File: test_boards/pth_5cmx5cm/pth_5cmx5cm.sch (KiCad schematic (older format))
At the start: 4 parts, among them Q1 BC560, Q2 2N3904

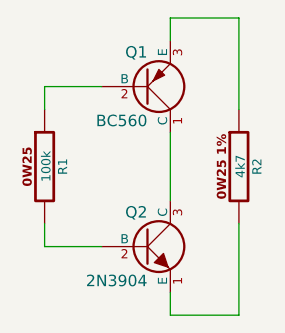
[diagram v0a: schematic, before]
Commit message: updating test board.
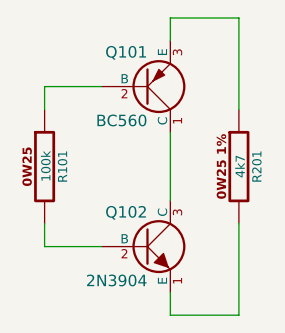
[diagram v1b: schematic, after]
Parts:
- removed Q1: BC560, ~, symbol BC560
- removed Q2: 2N3904, ~, symbol 2N3904
- added Q101: BC560, ~, symbol BC560
- added Q102: 2N3904, ~, symbol 2N3904
- renumbered R1 to R101, R2 to R201
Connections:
- net at R101.1: now also Q101.2 (B)
- net at R101.2: now also Q102.2 (B)
- net at R201.1: now also Q101.3 (E)
- net at R201.2: now also Q102.1 (E)
- new net: Q101.1 (C), Q102.3 (C)
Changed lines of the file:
@@
 $EndDescr
 $Comp
-L R_0W25 R1
+L R_0W25 R101
 U 1 1 53133287
 P 3500 3250
-F 0 "R1" V 3580 3250 40  0000 C CNN
+F 0 "R101" V 3580 3250 40  0000 C CNN
 F 1 "100k" V 3507 3251 40  0000 C CNN
 F 2 "~" V 3430 3250 30  0000 C CNN
@@
 $EndComp
 $Comp
-L R_0W25_1PCT R2
+L R_0W25_1PCT R201
 U 1 1 53133298
 P 4350 3250
-F 0 "R2" V 4430 3250 40  0000 C CNN
+F 0 "R201" V 4430 3250 40  0000 C CNN
 F 1 "4k7" V 4357 3251 40  0000 C CNN
 F 2 "~" V 4280 3250 30  0000 C CNN
 F 3 "~" H 4350 3250 30  0000 C CNN
 	1    4350 3250
-	1    0    0    -1
-$EndComp
-$Comp
-L 2N3904 Q2
-U 1 1 531332C1
-P 3950 3600
-F 0 "Q2" H 3950 3750 50  0000 R CNN
-F 1 "2N3904" H 3950 3450 50  0000 R CNN
-F 2 "~" H 3950 3600 60  0000 C CNN
-F 3 "~" H 3950 3600 60  0000 C CNN
-	1    3950 3600
-	1    0    0    -1
-$EndComp
-$Comp
-L BC560 Q1
-U 1 1 531332D2
-P 3950 2900
-F 0 "Q1" H 3950 3050 50  0000 R CNN
-F 1 "BC560" H 3950 2750 50  0000 R CNN
-F 2 "~" H 3950 2900 60  0000 C CNN
-F 3 "~" H 3950 2900 60  0000 C CNN
-	1    3950 2900
 	1    0    0    -1
 $EndComp
@@
 Wire Wire Line
 	4050 3900 4050 3800
+$Comp
+L 2N3904 Q102
+U 1 1 53134C44
+P 3950 3600
+F 0 "Q102" H 3950 3750 50  0000 R CNN
+F 1 "2N3904" H 3950 3450 50  0000 R CNN
+F 2 "~" H 3950 3600 60  0000 C CNN
+F 3 "~" H 3950 3600 60  0000 C CNN
+	1    3950 3600
+	1    0    0    -1
+$EndComp
+$Comp
+L BC560 Q101
+U 1 1 53134C53
+P 3950 2900
+F 0 "Q101" H 3950 3050 50  0000 R CNN
+F 1 "BC560" H 3950 2750 50  0000 R CNN
+F 2 "~" H 3950 2900 60  0000 C CNN
+F 3 "~" H 3950 2900 60  0000 C CNN
+	1    3950 2900
+	1    0    0    -1
+$EndComp
 $EndSCHEMATC

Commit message: adding mounting hole footprint, updating test board.
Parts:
- added H101, H102, H103, H104: HOLE, ~, symbol HOLE
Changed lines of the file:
@@
 LIBS:resistors_PL
 LIBS:transistors_PL
+LIBS:mounting_holes_PL
 LIBS:power
 LIBS:device
@@
 	1    0    0    -1
 $EndComp
+$Comp
+L HOLE H101
+U 1 1 53135434
+P 600 7650
+F 0 "H101" H 600 7705 40  0000 C CNN
+F 1 "HOLE" H 600 7590 30  0000 C CNN
+F 2 "~" H 600 7650 60  0000 C CNN
+F 3 "~" H 600 7650 60  0000 C CNN
+	1    600  7650
+	1    0    0    -1
+$EndComp
+$Comp
+L HOLE H102
+U 1 1 53135441
+P 800 7650
+F 0 "H102" H 800 7705 40  0000 C CNN
+F 1 "HOLE" H 800 7590 30  0000 C CNN
+F 2 "~" H 800 7650 60  0000 C CNN
+F 3 "~" H 800 7650 60  0000 C CNN
+	1    800  7650
+	1    0    0    -1
+$EndComp
+$Comp
+L HOLE H103
+U 1 1 53135447
+P 1000 7650
+F 0 "H103" H 1000 7705 40  0000 C CNN
+F 1 "HOLE" H 1000 7590 30  0000 C CNN
+F 2 "~" H 1000 7650 60  0000 C CNN
+F 3 "~" H 1000 7650 60  0000 C CNN
+	1    1000 7650
+	1    0    0    -1
+$EndComp
+$Comp
+L HOLE H104
+U 1 1 5313544D
+P 1200 7650
+F 0 "H104" H 1200 7705 40  0000 C CNN
+F 1 "HOLE" H 1200 7590 30  0000 C CNN
+F 2 "~" H 1200 7650 60  0000 C CNN
+F 3 "~" H 1200 7650 60  0000 C CNN
+	1    1200 7650
+	1    0    0    -1
+$EndComp

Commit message: updating test board (trying out tweaked pad settings)
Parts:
- added U101: 4N35, DIP6, symbol 4N35
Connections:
- net labels added: GND
- wire segments 11 -> 25
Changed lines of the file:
@@
 EESchema Schematic File Version 2
+LIBS:mounting_holes_PL
+LIBS:transistors_PL
+LIBS:opto_PL
 LIBS:resistors_PL
-LIBS:transistors_PL
-LIBS:mounting_holes_PL
 LIBS:power
 LIBS:device
@@
 	1    0    0    -1
 $EndComp
+$Comp
+L 4N35 U101
+U 1 1 5313A192
+P 5000 3250
+F 0 "U101" H 4745 3430 40  0000 L CNN
+F 1 "4N35" H 5260 3060 40  0000 R CNN
+F 2 "DIP6" H 4745 3065 29  0000 L CNN
+F 3 "~" H 5000 3250 60  0000 C CNN
+	1    5000 3250
+	1    0    0    -1
+$EndComp
+$Comp
+L GND #PWR01
+U 1 1 5313A1A1
+P 4200 4000
+F 0 "#PWR01" H 4200 4000 30  0001 C CNN
+F 1 "GND" H 4200 3930 30  0001 C CNN
+F 2 "" H 4200 4000 60  0000 C CNN
+F 3 "" H 4200 4000 60  0000 C CNN
+	1    4200 4000
+	1    0    0    -1
+$EndComp
+Wire Wire Line
+	4200 4000 4200 3900
+Connection ~ 4200 3900
+Wire Wire Line
+	4650 3150 4650 2900
+Wire Wire Line
+	4650 2900 4350 2900
+Connection ~ 4350 2900
+Wire Wire Line
+	5350 3250 5450 3250
+Wire Wire Line
+	5450 3250 5450 3550
+Wire Wire Line
+	5450 3550 4550 3550
+Wire Wire Line
+	4550 3550 4550 3350
+Wire Wire Line
+	4550 3350 4650 3350
+Wire Wire Line
+	5350 3150 5450 3150
+Wire Wire Line
+	5450 3150 5450 2800
+Wire Wire Line
+	5450 2800 4200 2800
+Wire Wire Line
+	4200 2800 4200 3250
+Wire Wire Line
+	4200 3250 4050 3250
+Connection ~ 4050 3250
+Wire Wire Line
+	5350 3350 5350 3400
+$Comp
+L GND #PWR02
+U 1 1 5313A214
+P 5350 3400
+F 0 "#PWR02" H 5350 3400 30  0001 C CNN
+F 1 "GND" H 5350 3330 30  0001 C CNN
+F 2 "" H 5350 3400 60  0000 C CNN
+F 3 "" H 5350 3400 60  0000 C CNN
+	1    5350 3400
+	1    0    0    -1
+$EndComp
